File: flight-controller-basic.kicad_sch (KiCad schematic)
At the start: 0 parts

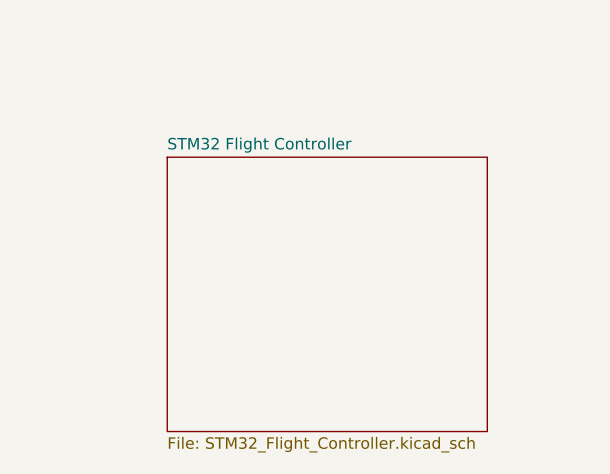
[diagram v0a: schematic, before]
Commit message: Fixed naming issue for the micro controller
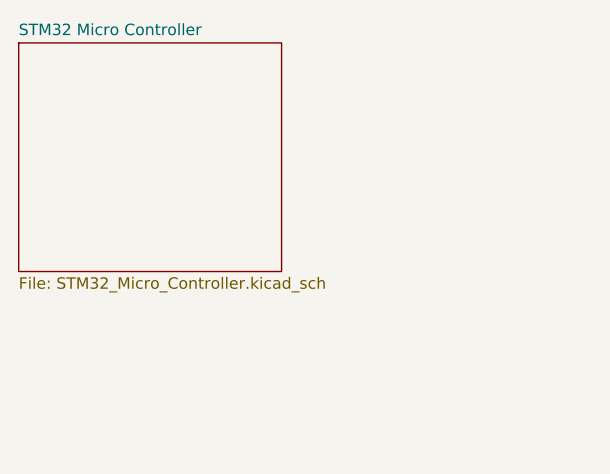
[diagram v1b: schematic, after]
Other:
- removed sheet STM32 Flight Controller
- added sheet STM32 Micro Controller (STM32_Micro_Controller.kicad_sch)
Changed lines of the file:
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@@
 	(paper "A4")
 	(sheet
-		(at 50.8 46.99)
-		(size 35.56 30.48)
+		(at 34.29 34.29)
+		(size 29.21 25.4)
 		(exclude_from_sim no)
 		(in_bom yes)
@@
 			(color 0 0 0 0.0000)
 		)
-		(property "Sheetname" "STM32 Flight Controller"
-			(at 50.8 46.2784 0)
+		(property "Sheetname" "STM32 Micro Controller"
+			(at 34.29 33.5784 0)
 			(effects
 				(font
@@
 			)
 		)
-		(property "Sheetfile" "STM32_Flight_Controller.kicad_sch"
-			(at 50.8 78.0546 0)
+		(property "Sheetfile" "STM32_Micro_Controller.kicad_sch"
+			(at 34.29 60.2746 0)
 			(effects
 				(font

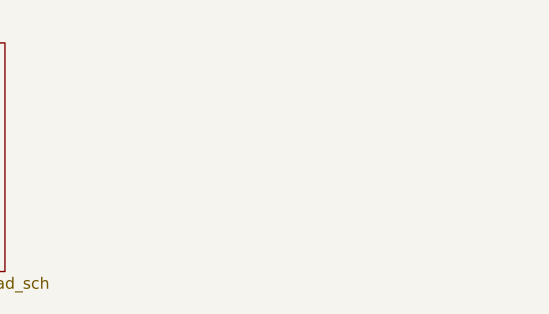
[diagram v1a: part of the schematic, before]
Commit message: Added the sensors section to the flight controller schematics.
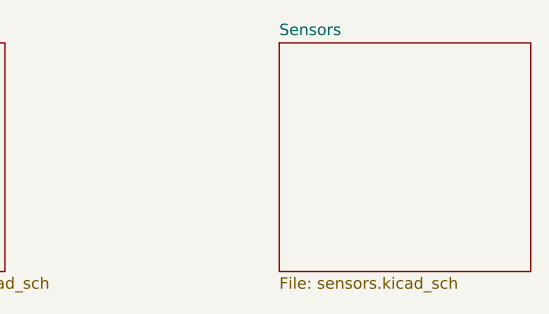
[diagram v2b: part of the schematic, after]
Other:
- added sheet Sensors (sensors.kicad_sch)
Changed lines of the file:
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@@
+		)
+	)
+	(sheet
+		(at 93.98 34.29)
+		(size 27.94 25.4)
+		(exclude_from_sim no)
+		(in_bom yes)
+		(on_board yes)
+		(dnp no)
+		(fields_autoplaced yes)
+		(stroke
+			(width 0.1524)
+			(type solid)
+		)
+		(fill
+			(color 0 0 0 0.0000)
+		)
+		(property "Sheetname" "Sensors"
+			(at 93.98 33.5784 0)
+			(effects
+				(font
+					(size 1.27 1.27)
+				)
+				(justify left bottom)
+			)
+		)
+		(property "Sheetfile" "sensors.kicad_sch"
+			(at 93.98 60.2746 0)
+			(effects
+				(font
+					(size 1.27 1.27)
+				)
+				(justify left top)
+			)
+		)
+		(instances
+			(project "flight-controller-basic"
+				(path "/e04fbe87-dc7c-407c-abef-b71ed1bbe06a"
+					(page "3")
+				)
+			)
 		)
 	)

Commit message: Add files via upload
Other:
- removed sheet Sensors
- added sheet GPS (omnia_FC_2026/IMU_FC_G/GP_GPS/GP_GPS.kicad_sch)
- added sheet sensors (sensors.kicad_sch)
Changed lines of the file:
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@@
 	(paper "A4")
+	(sheet
+		(at 34.29 66.04)
+		(size 30.48 25.4)
+		(exclude_from_sim no)
+		(in_bom yes)
+		(on_board yes)
+		(dnp no)
+		(fields_autoplaced yes)
+		(stroke
+			(width 0.1524)
+			(type solid)
+		)
+		(fill
+			(color 0 0 0 0.0000)
+		)
+		(property "Sheetname" "sensors"
+			(at 34.29 65.3284 0)
+			(effects
+				(font
+					(size 1.27 1.27)
+				)
+				(justify left bottom)
+			)
+		)
+		(property "Sheetfile" "sensors.kicad_sch"
+			(at 34.29 92.0246 0)
+			(effects
+				(font
+					(size 1.27 1.27)
+				)
+				(justify left top)
+				(hide yes)
+			)
+		)
+		(instances
+			(project "flight-controller-basic"
+				(path "/e04fbe87-dc7c-407c-abef-b71ed1bbe06a"
+					(page "3")
+				)
+			)
+		)
+	)
 	(sheet
 		(at 34.29 34.29)
@@
 				)
 				(justify left top)
+				(hide yes)
 			)
 		)
@@
 	)
 	(sheet
-		(at 93.98 34.29)
-		(size 27.94 25.4)
+		(at 34.29 96.52)
+		(size 30.48 26.67)
 		(exclude_from_sim no)
 		(in_bom yes)
@@
 			(color 0 0 0 0.0000)
 		)
-		(property "Sheetname" "Sensors"
-			(at 93.98 33.5784 0)
+		(property "Sheetname" "GPS"
+			(at 34.29 95.8084 0)
 			(effects
 				(font
@@
 			)
 		)
-		(property "Sheetfile" "sensors.kicad_sch"
-			(at 93.98 60.2746 0)
+		(property "Sheetfile" "omnia_FC_2026/IMU_FC_G/GP_GPS/GP_GPS.kicad_sch"
+			(at 34.29 123.7746 0)
 			(effects
 				(font
@@
 				)
 				(justify left top)
+				(hide yes)
 			)
 		)
@@
 			(project "flight-controller-basic"
 				(path "/e04fbe87-dc7c-407c-abef-b71ed1bbe06a"
-					(page "3")
+					(page "4")
 				)
 			)
